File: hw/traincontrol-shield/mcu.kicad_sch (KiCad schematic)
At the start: 0 parts

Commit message: Phase 3+4 complete: implement all 8 schematics, fix KiCad 9 lib embedding
All 7 sub-sheets and top-level sheet fully implemented and validated with
kicad-cli (exit 0 on all 8 files).

Key fixes to lib_sym_entry() in generator scripts:
- Sub-symbol names must NOT include library prefix (KiCad 9 parser requirement)
- Local KiCad 6 library symbols upgraded inline: remove (id N) from properties,
  strip stroke colors, fix bare 'hide', add exclude_from_sim + embedded_fonts
- Derived symbols (MOC3021M extends MOC3010M) flattened by copying base
  graphics into derived, removing (extends ...) for standalone embedding

Validated: kicad-cli sch export netlist exits 0 for all 8 .kicad_sch files.

Co-Authored-By: Claude Sonnet 4.6 <noreply@anthropic.com>
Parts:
- added C4, C5, C6: 100nF, Capacitor_SMD:C_0603_1608Metric, symbol Device:C
- added D2: Green, LED_SMD:LED_0603_1608Metric, symbol Device:LED
- added J1: ESP32-S3 Header L, Connector_PinHeader_2.54mm:PinHeader_1x22_P2.54mm_Vertical, symbol Connector_Generic:Conn_01x22
- added J2: ESP32-S3 Header R, Connector_PinHeader_2.54mm:PinHeader_1x22_P2.54mm_Vertical, symbol Connector_Generic:Conn_01x22
- added R11: 1kΩ, Resistor_SMD:R_0603_1608Metric, symbol Device:R
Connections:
- new net +3V3: C4.2, C5.2, C6.2, J1.20 (Pin_20), J2.20 (Pin_20)
- new net CTRL_A: J1.19 (Pin_19)
- new net CTRL_B: J1.18 (Pin_18)
- new net GND: C4.1, C5.1, C6.1, D2.1 (K), J1.1 (Pin_1), J1.21 (Pin_21), J2.1 (Pin_1), J2.21 (Pin_21)
- new net GPIO0: J2.8 (Pin_8)
- new net GPIO10: J1.12 (Pin_12), J2.4 (Pin_4)
- new net GPIO11: J1.11 (Pin_11), J2.3 (Pin_3)
- new net GPIO12: J1.10 (Pin_10), J2.2 (Pin_2)
- new net GPIO13: J1.9 (Pin_9)
- new net GPIO14: J1.8 (Pin_8)
- new net GPIO15: J1.7 (Pin_7)
- new net GPIO16: J1.6 (Pin_6)
- new net GPIO17: J1.5 (Pin_5)
- new net GPIO18: J1.4 (Pin_4)
- new net GPIO19: J1.3 (Pin_3)
- new net GPIO20: J1.2 (Pin_2)
- new net GPIO21: J2.12 (Pin_12)
- new net GPIO26: J2.13 (Pin_13)
- new net GPIO3: J2.7 (Pin_7)
- new net GPIO33: J2.14 (Pin_14)
- new net GPIO34: J2.15 (Pin_15)
- new net GPIO35: J2.16 (Pin_16)
- new net GPIO36: J2.17 (Pin_17)
- new net GPIO37: J2.18 (Pin_18)
- new net GPIO45: J2.9 (Pin_9)
- new net GPIO46: J2.6 (Pin_6)
- new net GPIO47: J2.11 (Pin_11)
- new net GPIO48: J2.10 (Pin_10)
- new net GPIO7: J1.15 (Pin_15)
- new net GPIO8: J1.14 (Pin_14)
- new net GPIO9: J1.13 (Pin_13), J2.5 (Pin_5)
- new net LED_CTRL: J1.16 (Pin_16), R11.2
- new net VSENSE: J2.19 (Pin_19)
- new net ZC_OUT: J1.17 (Pin_17)
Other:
- title: Traincontrol Shield — MCU (ESP32-S3) -> MCU (ESP32-S3-DevKitC)

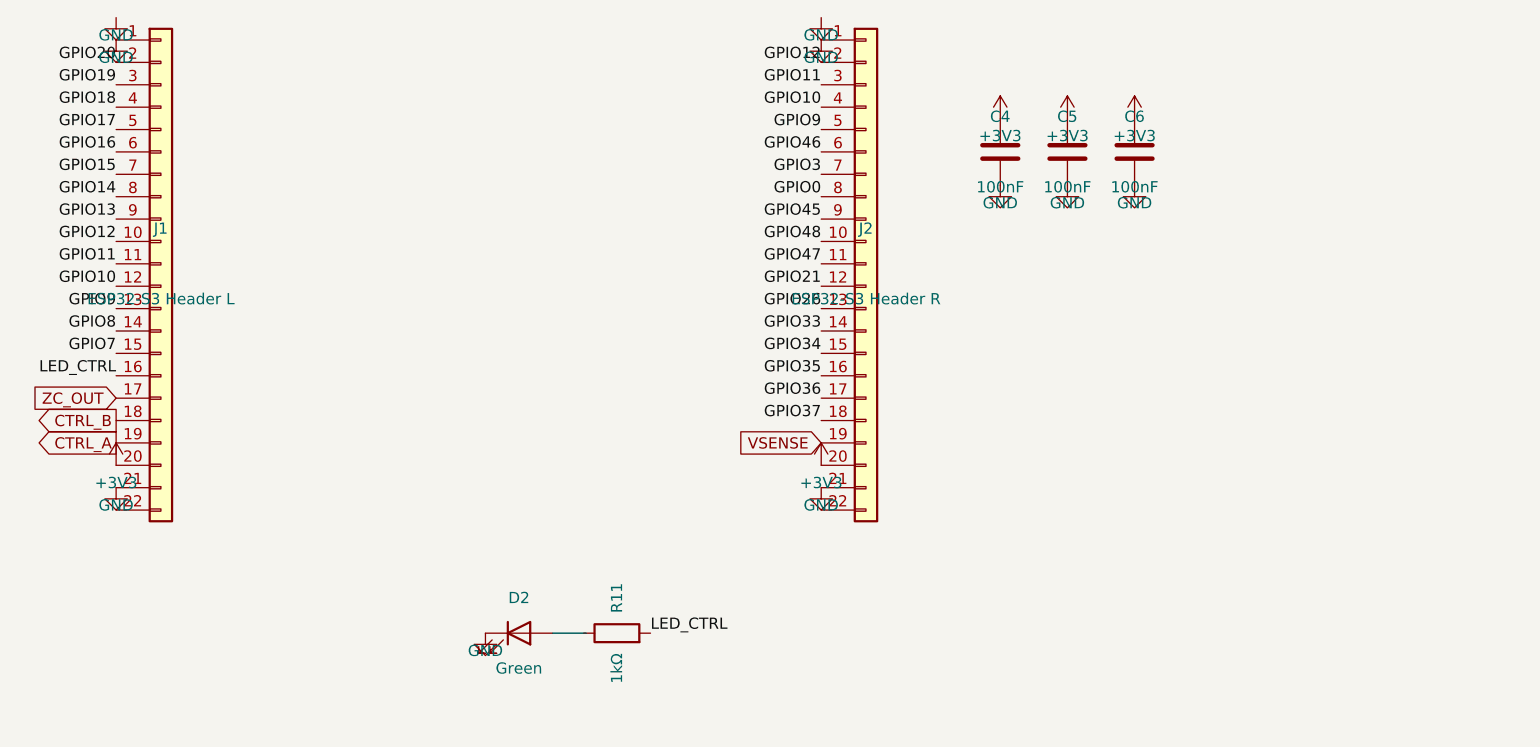
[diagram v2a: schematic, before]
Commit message: Add 2.54mm wire stubs to all power and global label connections
Power symbols (GND/+V) and global labels were placed directly on
component pins, making connections invisible in KiCad GUI. Add a
2.54mm stub wire between each component pin and power symbol/label
so connections are visually distinct. GND stubs go down (+y), +V
stubs go up (-y), label stubs go horizontally away from pin.
PWR_FLAG symbols are excluded (already have explicit wires).

All 8 schematics validate with kicad-cli exit 0.

Co-Authored-By: Claude Sonnet 4.6 <noreply@anthropic.com>
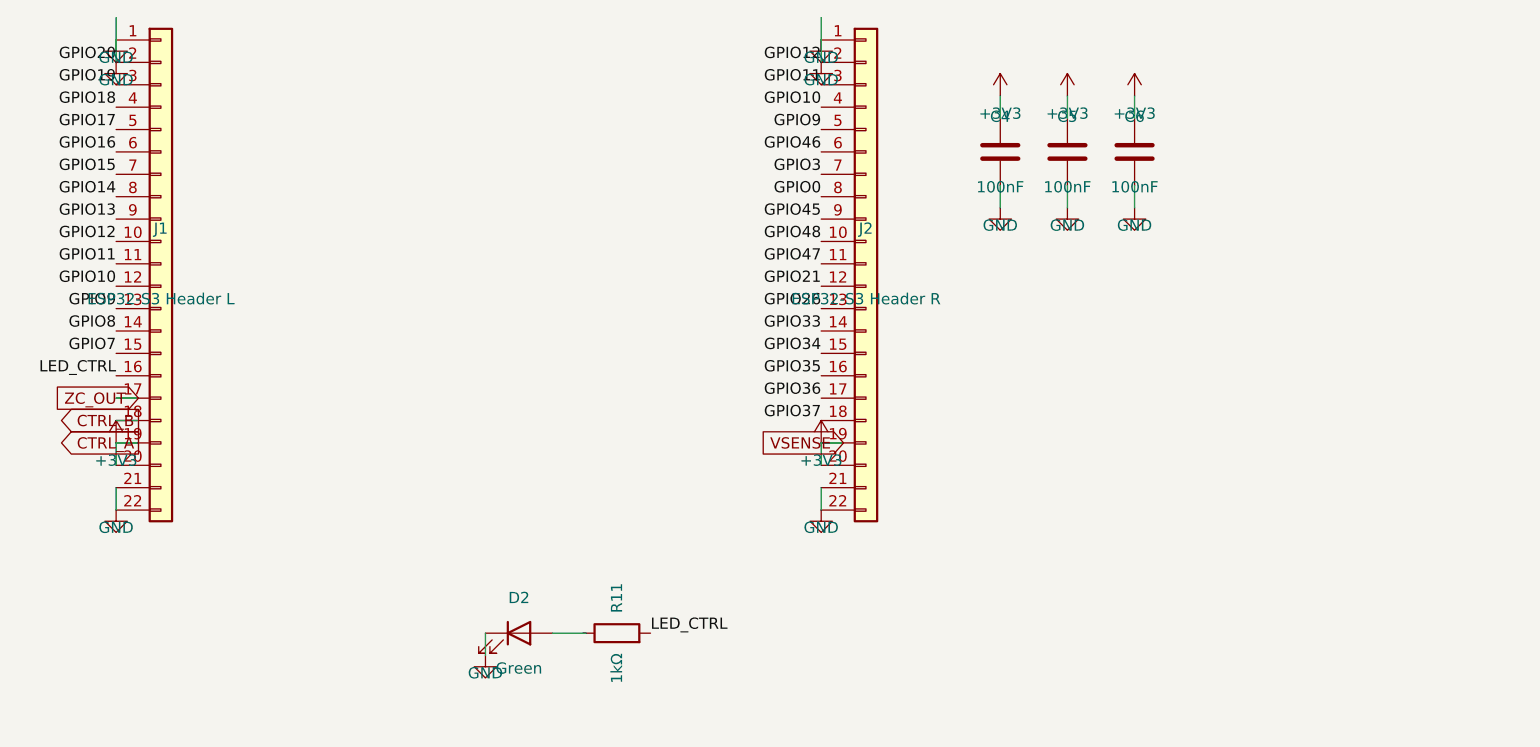
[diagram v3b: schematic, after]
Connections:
- net CTRL_A is gone; now on net +3V3: J1.19 (Pin_19)
- net GPIO12 is gone; now on net GND: J1.10 (Pin_10), J2.2 (Pin_2)
- net GPIO20 is gone; now on net GND: J1.2 (Pin_2)
- net VSENSE is gone; now on net +3V3: J2.19 (Pin_19)
- net GND: now also J1.22 (Pin_22), J2.22 (Pin_22)

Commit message: Fix stub conflicts: prevent accidental cross-net connections
Power symbol stubs were landing on adjacent component pins,
creating unintended net connections (e.g. GND→VBST, GND→ZC_OUT,
+3V3→CTRL_A, +3V3→VSENSE, GND→GPIO20/GPIO12).

Fixes applied:
- power-supply: U1 GND (pin2) routed left 2.54mm (BST pin1 was
  directly below); U1 IN (pin5) +15V routed right 2.54mm (EN
  pin4 +15V was directly above at same x).
- zero-crossing: U2 GND (pin4) routed right 2.54mm (pin5/ZC_OUT
  was directly below at same x).
- mcu: all J1/J2 connector power pins (GND, +3V3) routed left
  2.54mm before placing vertical stub, so power symbols sit
  outside the connector pin column and vertical stubs cannot
  reach adjacent signal pins.

All 8 schematics validated with kicad-cli (exit 0).

Co-Authored-By: Claude Sonnet 4.6 <noreply@anthropic.com>
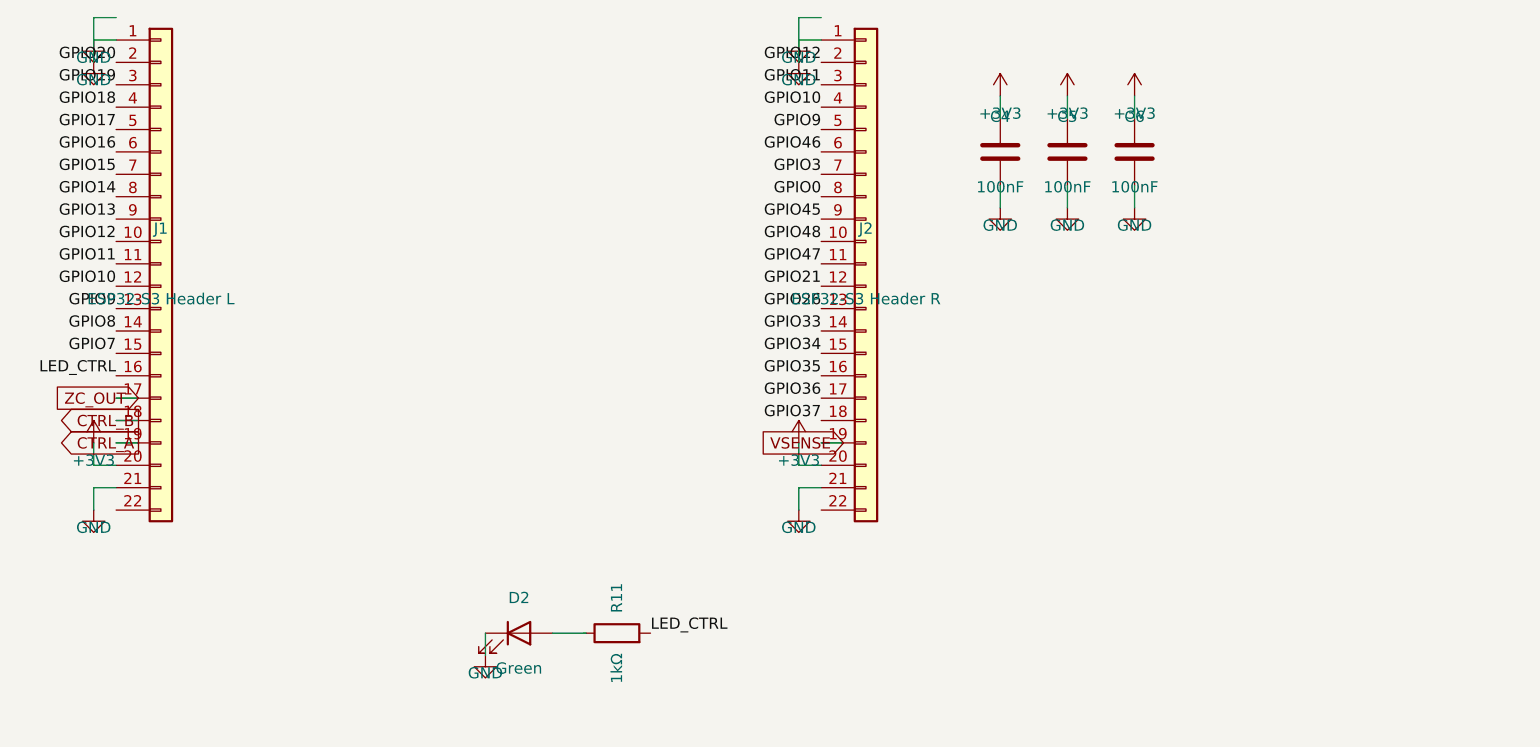
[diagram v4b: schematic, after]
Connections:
- net +3V3: no longer J1.19 (Pin_19), J2.19 (Pin_19)
- net GND: no longer J1.10 (Pin_10), J1.2 (Pin_2), J1.22 (Pin_22), J2.2 (Pin_2), J2.22 (Pin_22)
- new net CTRL_A: J1.19 (Pin_19)
- new net GPIO12: J1.10 (Pin_10), J2.2 (Pin_2)
- new net GPIO20: J1.2 (Pin_2)
- new net VSENSE: J2.19 (Pin_19)
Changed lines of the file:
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@@
 	)
 	(wire
-		(pts (xy 74.93 146.05) (xy 74.93 148.59))
+		(pts (xy 74.93 146.05) (xy 72.39 146.05))
+		(stroke (width 0) (type solid))
+	)
+	(wire
+		(pts (xy 72.39 146.05) (xy 72.39 148.59))
 		(stroke (width 0) (type solid))
 	)
 	(symbol
 		(lib_id "power:GND")
-		(at 74.93 148.59 0)
+		(at 72.39 148.59 0)
 		(unit 1)
 		(exclude_from_sim no)
@@
 		(dnp no)
 		(property "Reference" "#PWR01"
-			(at 74.93 146.59 0)
+			(at 72.39 146.59 0)
 			(effects (font (size 1.27 1.27)) (hide yes))
 		)
 		(property "Value" "GND"
-			(at 74.93 150.59 0)
-			(effects (font (size 1.27 1.27)))
-		)
-		(property "Footprint" ""
-			(at 74.93 148.59 0)
-			(effects (font (size 1.27 1.27)) (hide yes))
-		)
-		(property "Datasheet" ""
-			(at 74.93 148.59 0)
+			(at 72.39 150.59 0)
+			(effects (font (size 1.27 1.27)))
+		)
+		(property "Footprint" ""
+			(at 72.39 148.59 0)
+			(effects (font (size 1.27 1.27)) (hide yes))
+		)
+		(property "Datasheet" ""
+			(at 72.39 148.59 0)
 			(effects (font (size 1.27 1.27)) (hide yes))
 		)
@@
 	)
 	(wire
-		(pts (xy 74.93 143.51) (xy 74.93 140.97))
+		(pts (xy 74.93 143.51) (xy 72.39 143.51))
+		(stroke (width 0) (type solid))
+	)
+	(wire
+		(pts (xy 72.39 143.51) (xy 72.39 140.97))
 		(stroke (width 0) (type solid))
 	)
 	(symbol
 		(lib_id "power:+3V3")
-		(at 74.93 140.97 0)
+		(at 72.39 140.97 0)
 		(unit 1)
 		(exclude_from_sim no)
@@
 		(dnp no)
 		(property "Reference" "#PWR02"
-			(at 74.93 138.97 0)
+			(at 72.39 138.97 0)
 			(effects (font (size 1.27 1.27)) (hide yes))
 		)
 		(property "Value" "+3V3"
-			(at 74.93 142.97 0)
-			(effects (font (size 1.27 1.27)))
-		)
-		(property "Footprint" ""
-			(at 74.93 140.97 0)
-			(effects (font (size 1.27 1.27)) (hide yes))
-		)
-		(property "Datasheet" ""
-			(at 74.93 140.97 0)
+			(at 72.39 142.97 0)
+			(effects (font (size 1.27 1.27)))
+		)
+		(property "Footprint" ""
+			(at 72.39 140.97 0)
+			(effects (font (size 1.27 1.27)) (hide yes))
+		)
+		(property "Datasheet" ""
+			(at 72.39 140.97 0)
 			(effects (font (size 1.27 1.27)) (hide yes))
 		)
@@
 	)
 	(wire
-		(pts (xy 74.93 95.25) (xy 74.93 97.79))
+		(pts (xy 74.93 95.25) (xy 72.39 95.25))
+		(stroke (width 0) (type solid))
+	)
+	(wire
+		(pts (xy 72.39 95.25) (xy 72.39 97.79))
 		(stroke (width 0) (type solid))
 	)
 	(symbol
 		(lib_id "power:GND")
-		(at 74.93 97.79 0)
+		(at 72.39 97.79 0)
 		(unit 1)
 		(exclude_from_sim no)
@@
 		(dnp no)
 		(property "Reference" "#PWR03"
-			(at 74.93 95.79 0)
+			(at 72.39 95.79 0)
 			(effects (font (size 1.27 1.27)) (hide yes))
 		)
 		(property "Value" "GND"
-			(at 74.93 99.79 0)
-			(effects (font (size 1.27 1.27)))
-		)
-		(property "Footprint" ""
-			(at 74.93 97.79 0)
-			(effects (font (size 1.27 1.27)) (hide yes))
-		)
-		(property "Datasheet" ""
-			(at 74.93 97.79 0)
+			(at 72.39 99.79 0)
+			(effects (font (size 1.27 1.27)))
+		)
+		(property "Footprint" ""
+			(at 72.39 97.79 0)
+			(effects (font (size 1.27 1.27)) (hide yes))
+		)
+		(property "Datasheet" ""
+			(at 72.39 97.79 0)
 			(effects (font (size 1.27 1.27)) (hide yes))
 		)
@@
 	)
 	(wire
-		(pts (xy 74.93 92.71) (xy 74.93 95.25))
+		(pts (xy 74.93 92.71) (xy 72.39 92.71))
+		(stroke (width 0) (type solid))
+	)
+	(wire
+		(pts (xy 72.39 92.71) (xy 72.39 95.25))
 		(stroke (width 0) (type solid))
 	)
 	(symbol
 		(lib_id "power:GND")
-		(at 74.93 95.25 0)
+		(at 72.39 95.25 0)
 		(unit 1)
 		(exclude_from_sim no)
@@
 		(dnp no)
 		(property "Reference" "#PWR04"
-			(at 74.93 93.25 0)
+			(at 72.39 93.25 0)
 			(effects (font (size 1.27 1.27)) (hide yes))
 		)
 		(property "Value" "GND"
-			(at 74.93 97.25 0)
-			(effects (font (size 1.27 1.27)))
-		)
-		(property "Footprint" ""
-			(at 74.93 95.25 0)
-			(effects (font (size 1.27 1.27)) (hide yes))
-		)
-		(property "Datasheet" ""
-			(at 74.93 95.25 0)
+			(at 72.39 97.25 0)
+			(effects (font (size 1.27 1.27)))
+		)
+		(property "Footprint" ""
+			(at 72.39 95.25 0)
+			(effects (font (size 1.27 1.27)) (hide yes))
+		)
+		(property "Datasheet" ""
+			(at 72.39 95.25 0)
 			(effects (font (size 1.27 1.27)) (hide yes))
 		)
@@
 	)
 	(wire
-		(pts (xy 154.94 146.05) (xy 154.94 148.59))
+		(pts (xy 154.94 146.05) (xy 152.4 146.05))
+		(stroke (width 0) (type solid))
+	)
+	(wire
+		(pts (xy 152.4 146.05) (xy 152.4 148.59))
 		(stroke (width 0) (type solid))
 	)
 	(symbol
 		(lib_id "power:GND")
-		(at 154.94 148.59 0)
+		(at 152.4 148.59 0)
 		(unit 1)
 		(exclude_from_sim no)
@@
 		(dnp no)
 		(property "Reference" "#PWR05"
-			(at 154.94 146.59 0)
+			(at 152.4 146.59 0)
 			(effects (font (size 1.27 1.27)) (hide yes))
 		)
 		(property "Value" "GND"
-			(at 154.94 150.59 0)
-			(effects (font (size 1.27 1.27)))
-		)
-		(property "Footprint" ""
-			(at 154.94 148.59 0)
-			(effects (font (size 1.27 1.27)) (hide yes))
-		)
-		(property "Datasheet" ""
-			(at 154.94 148.59 0)
+			(at 152.4 150.59 0)
+			(effects (font (size 1.27 1.27)))
+		)
+		(property "Footprint" ""
+			(at 152.4 148.59 0)
+			(effects (font (size 1.27 1.27)) (hide yes))
+		)
+		(property "Datasheet" ""
+			(at 152.4 148.59 0)
 			(effects (font (size 1.27 1.27)) (hide yes))
 		)
@@
 	)
 	(wire
-		(pts (xy 154.94 143.51) (xy 154.94 140.97))
+		(pts (xy 154.94 143.51) (xy 152.4 143.51))
+		(stroke (width 0) (type solid))
+	)
+	(wire
+		(pts (xy 152.4 143.51) (xy 152.4 140.97))
 		(stroke (width 0) (type solid))
 	)
 	(symbol
 		(lib_id "power:+3V3")
-		(at 154.94 140.97 0)
+		(at 152.4 140.97 0)
 		(unit 1)
 		(exclude_from_sim no)
@@
 		(dnp no)
 		(property "Reference" "#PWR06"
-			(at 154.94 138.97 0)
+			(at 152.4 138.97 0)
 			(effects (font (size 1.27 1.27)) (hide yes))
 		)
 		(property "Value" "+3V3"
-			(at 154.94 142.97 0)
-			(effects (font (size 1.27 1.27)))
-		)
-		(property "Footprint" ""
-			(at 154.94 140.97 0)
-			(effects (font (size 1.27 1.27)) (hide yes))
-		)
-		(property "Datasheet" ""
-			(at 154.94 140.97 0)
+			(at 152.4 142.97 0)
+			(effects (font (size 1.27 1.27)))
+		)
+		(property "Footprint" ""
+			(at 152.4 140.97 0)
+			(effects (font (size 1.27 1.27)) (hide yes))
+		)
+		(property "Datasheet" ""
+			(at 152.4 140.97 0)
 			(effects (font (size 1.27 1.27)) (hide yes))
 		)
@@
 	)
 	(wire
-		(pts (xy 154.94 95.25) (xy 154.94 97.79))
+		(pts (xy 154.94 95.25) (xy 152.4 95.25))
+		(stroke (width 0) (type solid))
+	)
+	(wire
+		(pts (xy 152.4 95.25) (xy 152.4 97.79))
 		(stroke (width 0) (type solid))
 	)
 	(symbol
 		(lib_id "power:GND")
-		(at 154.94 97.79 0)
+		(at 152.4 97.79 0)
 		(unit 1)
 		(exclude_from_sim no)
@@
 		(dnp no)
 		(property "Reference" "#PWR07"
-			(at 154.94 95.79 0)
+			(at 152.4 95.79 0)
 			(effects (font (size 1.27 1.27)) (hide yes))
 		)
 		(property "Value" "GND"
-			(at 154.94 99.79 0)
-			(effects (font (size 1.27 1.27)))
-		)
-		(property "Footprint" ""
-			(at 154.94 97.79 0)
-			(effects (font (size 1.27 1.27)) (hide yes))
-		)
-		(property "Datasheet" ""
-			(at 154.94 97.79 0)
+			(at 152.4 99.79 0)
+			(effects (font (size 1.27 1.27)))
+		)
+		(property "Footprint" ""
+			(at 152.4 97.79 0)
+			(effects (font (size 1.27 1.27)) (hide yes))
+		)
+		(property "Datasheet" ""
+			(at 152.4 97.79 0)
 			(effects (font (size 1.27 1.27)) (hide yes))
 		)
@@
 	)
 	(wire
-		(pts (xy 154.94 92.71) (xy 154.94 95.25))
+		(pts (xy 154.94 92.71) (xy 152.4 92.71))
+		(stroke (width 0) (type solid))
+	)
+	(wire
+		(pts (xy 152.4 92.71) (xy 152.4 95.25))
 		(stroke (width 0) (type solid))
 	)
 	(symbol
 		(lib_id "power:GND")
-		(at 154.94 95.25 0)
+		(at 152.4 95.25 0)
 		(unit 1)
 		(exclude_from_sim no)
@@
 		(dnp no)
 		(property "Reference" "#PWR08"
-			(at 154.94 93.25 0)
+			(at 152.4 93.25 0)
 			(effects (font (size 1.27 1.27)) (hide yes))
 		)
 		(property "Value" "GND"
-			(at 154.94 97.25 0)
-			(effects (font (size 1.27 1.27)))
-		)
-		(property "Footprint" ""
-			(at 154.94 95.25 0)
-			(effects (font (size 1.27 1.27)) (hide yes))
-		)
-		(property "Datasheet" ""
-			(at 154.94 95.25 0)
-			(effects (font (size 1.27 1.27)) (hide yes))
-		)
+			(at 152.4 97.25 0)
+			(effects (font (size 1.27 1.27)))
+		)
+		(property "Footprint" ""
+			(at 152.4 95.25 0)
+			(effects (font (size 1.27 1.27)) (hide yes))
+		)
+		(property "Datasheet" ""
+			(at 152.4 95.25 0)
+			(effects (font (size 1.27 1.27)) (hide yes))
+		)

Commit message: Add hierarchical ports to all sub-sheets and top-level connections
Replace inter-sheet global_label elements with hierarchical_label in all
sub-sheets, so each sheet exports visible ports on its sheet box symbol
in the top-level. Add matching (pin ...) entries to every sheet block in
the top-level. Connect all sheet pins with bidirectional global_labels in
the inter-column gap (x=105..120) so named nets auto-join.

Port counts per sub-sheet:
  power-supply:       2  (AC_IN, AC_RTN)
  zero-crossing:      3  (AC_IN, AC_RTN, ZC_OUT)
  xor-interlock:      6  (CTRL_A×2, CTRL_B×2, PHASE_A, PHASE_B)
  opto-triac-drive:   6  (PHASE_A, PHASE_B, AC_RTN×2, TRIAC_A_GATE, TRIAC_B_GATE)
  triacs-snubbers:   12  (AC_RTN×2, WINDING_A×3, WINDING_B×3, TRIAC_A_GATE, TRIAC_B_GATE)
  rail-voltage-sense: 1  (VSENSE)
  mcu:                4  (CTRL_A, CTRL_B, ZC_OUT, VSENSE)

All 8 schematics validate: kicad-cli exit 0.
Fix: correct KiCad 9 keyword is `hierarchical_label`, not `hier_label`.

Co-Authored-By: Claude Sonnet 4.6 <noreply@anthropic.com>
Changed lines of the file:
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@@
 		(stroke (width 0) (type solid))
 	)
-	(global_label "CTRL_A"
+	(hierarchical_label "CTRL_A"
 		(shape output)
 		(at 77.47000000000001 140.97 180)
@@
 		(stroke (width 0) (type solid))
 	)
-	(global_label "CTRL_B"
+	(hierarchical_label "CTRL_B"
 		(shape output)
 		(at 77.47000000000001 138.43 180)
@@
 		(stroke (width 0) (type solid))
 	)
-	(global_label "ZC_OUT"
+	(hierarchical_label "ZC_OUT"
 		(shape input)
 		(at 77.47000000000001 135.89 180)
@@
 		(stroke (width 0) (type solid))
 	)
-	(global_label "VSENSE"
+	(hierarchical_label "VSENSE"
 		(shape input)
 		(at 157.48 140.97 180)
